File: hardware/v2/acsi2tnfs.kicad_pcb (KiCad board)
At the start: 2 copper layers, 51.5 x 60.2 mm, 22 parts, among them J1 Conn_01x19, J3 To SD card, SW1 SW_Prev, U1 SN74LVC245APW, U2 SN74LVC245APW, U3 SN74LS07

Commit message: Hardware: v2 and v2-cable, drop v1 and dev
v2 (DB19 on the board) and the new v2-cable (flat cable to a Lotharek DB19
adapter, pass-through header) share one circuit: 74LS07 for /IRQ and /DRQ,
pull-ups on /OE and the 74LS07 inputs, no pull-ups on /IRQ and /DRQ (those
upset the floppy drive when the board is off). v2-cable's box headers are
numbered per row, so pin n is ACSI pin n like on the adapter. Each project
carries its own footprints and fp-lib-table. hardware/README.md explains
both boards. v1, dev and the old gerbers are gone.

Co-Authored-By: Claude Opus 5.5 <noreply@anthropic.com>
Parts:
- removed R1, R2: NC, Resistor_SMD:R_0805_2012Metric
- J1: value Conn_01x19 -> To ACSI
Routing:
- net /DRQ: track 28.1 -> 22.4 mm
- net +5V: track 62.8 -> 57.8 mm
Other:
- board text added: "Atari ST ASCI netdrive & harddisk emulator"
- board text added: "https://retroloft.net/projects/acsi2tnfs"

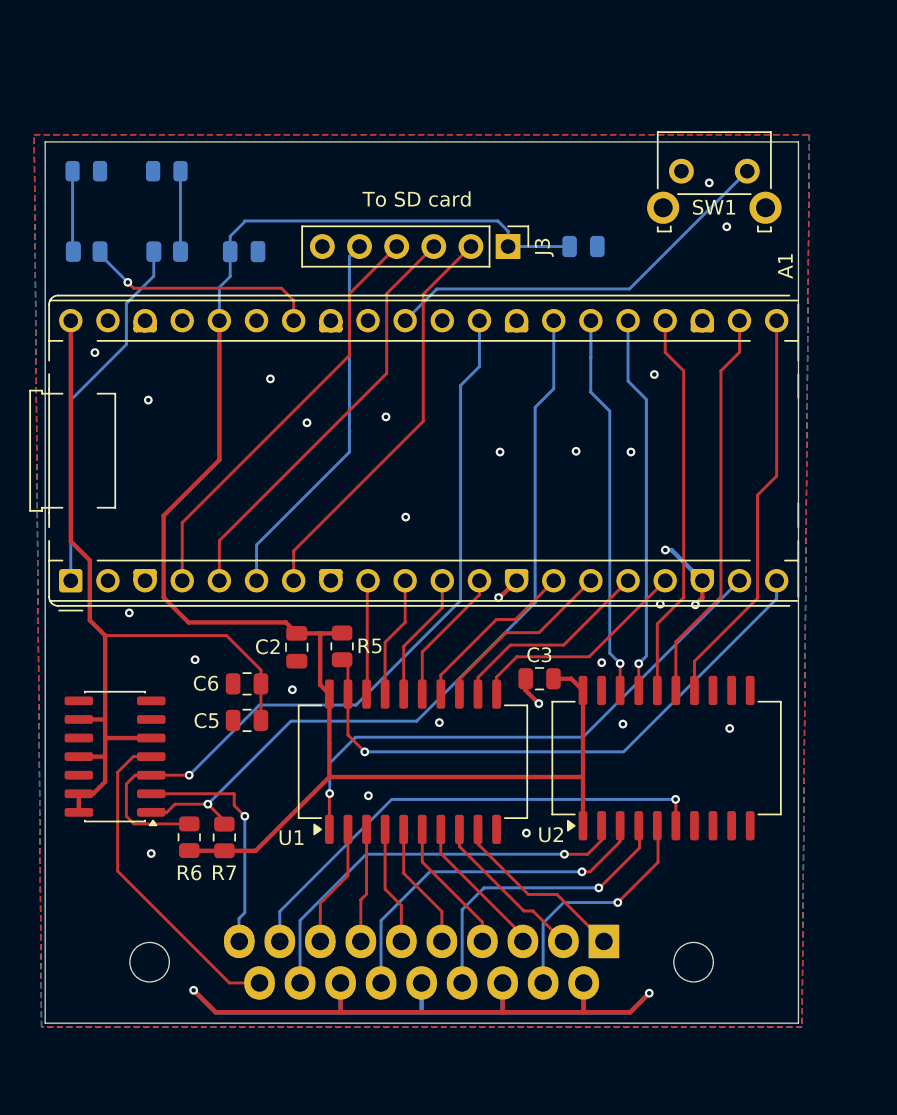
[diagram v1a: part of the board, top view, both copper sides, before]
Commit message: hardware/v2: TF-01A micro SD socket on the board, improved layout
Card1 uses the footprint from the project library; schema.pdf updated.

Co-Authored-By: Claude Opus 5.5 <noreply@anthropic.com>
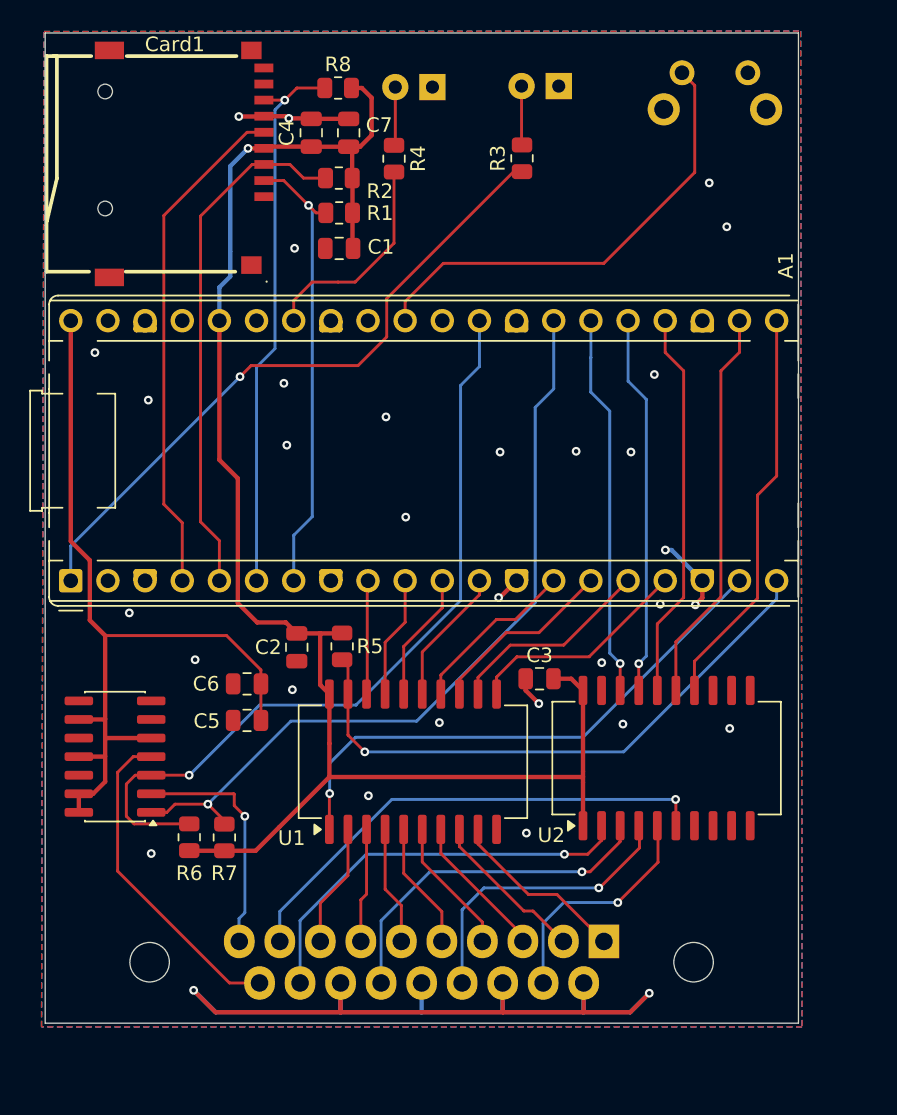
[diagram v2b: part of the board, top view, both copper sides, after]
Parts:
- removed J3: To SD card, Connector_PinHeader_2.54mm:PinHeader_1x06_P2.54mm_Vertical
- added C7: 10uF, Capacitor_SMD:C_0805_2012Metric, F.Cu at (131.0, 35.4)
- added Card1: TF-01A, ACSI Connector:TF-SMD_TF-01A, F.Cu at (119.9, 37.5)
- added R1: 10K, Resistor_SMD:R_0805_2012Metric, F.Cu at (130.3, 40.9)
- added R2: 10K, Resistor_SMD:R_0805_2012Metric, F.Cu at (130.3, 38.5)
- added R8: 10K, Resistor_SMD:R_0805_2012Metric, F.Cu at (130.3, 32.3)
- C1, R3, R4: moved to F.Cu
- C4: value 100n -> 100nF; moved to F.Cu
- D1, D2: footprint LED_SMD:LED_0805_2012Metric -> LED_THT:LED_D3.0mm
- SW1: moved to B.Cu
- moved D1 27.4 mm to (145.4, 32.2), turned to 180 degrees
- moved R3 25.1 mm to (142.8, 37.1), turned to -90 degrees
- moved D2 24.4 mm to (136.7, 32.2)
- moved R4 22.0 mm to (134.1, 37.1), turned to -90 degrees
- moved C4 20.2 mm to (128.4, 35.4), turned to 90 degrees
- moved SW1 8.12 mm to (158.3, 31.3), turned to 180 degrees
- moved C1 6.50 mm to (130.3, 43.3), turned to 180 degrees
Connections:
- A1 pad 4: CLK -> SCLK
- A1 pad 7: CS -> SD_CS
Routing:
- net SCLK: track 0.00 -> 34.7 mm
- net SD_CS: track 0.00 -> 31.4 mm, vias 0 -> 1
- net CLK: track 28.9 -> 0.00 mm
- net CS: track 27.9 -> 0.00 mm
- net POWER_LED: track 24.9 -> 45.4 mm, vias 0 -> 1
- net MISO: track 25.8 -> 38.2 mm, vias 0 -> 1
- net GND: track 88.5 -> 96.1 mm, vias 29 -> 32
- net MOSI: track 28.9 -> 35.9 mm
- net BUTTON: track 27.6 -> 31.9 mm
- net +3.3V: track 115.6 -> 111.3 mm, vias 0 -> 1
- net Net-(D2-A): track 5.52 -> 4.02 mm
- net Net-(D1-A): track 5.50 -> 4.04 mm
- net STATUS_LED: track 16.1 -> 14.7 mm, vias 1 -> 0
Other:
- board size 51.5 x 60.2 mm -> 51.5 x 67.7 mm
- board text added: "Mode"

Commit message: hardware: U1/U2 are 74LVC245ADW, silkscreen says ACSI
Both boards: the value of U1/U2 matches the SOIC-20W footprint, the
silkscreen text reads ACSI instead of ASCI, and a stray text outside the
v2 board is gone. schema.pdf and the 3D views updated.

Co-Authored-By: Claude Opus 5.5 <noreply@anthropic.com>
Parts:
- U1, U2: value SN74LVC245APW -> 74LVC245ADW
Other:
- board text added: "Atari ST ACSI netdrive & harddisk emulator"
- board text removed: "Atari ST ASCI netdrive & harddisk emulator"
- board text removed: "Atari ST ASCI netdrive and harddisk emulator"
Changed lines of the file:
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@@
 			)
 		)
-		(property "Value" "SN74LVC245APW"
+		(property "Value" "74LVC245ADW"
 			(at 0 8.66 90)
 			(layer "F.Fab")
@@
 			)
 		)
-		(property "Value" "SN74LVC245APW"
+		(property "Value" "74LVC245ADW"
 			(at 0 8.66 90)
 			(layer "F.Fab")
@@
 		(layer "Edge.Cuts")
 	)
-	(gr_text "Atari ST ASCI netdrive and harddisk emulator"
-		(at 200.5 144.5 0)
-		(layer "F.SilkS")
-		(effects
-			(font
-				(size 1.5 1.5)
-				(thickness 0.3)
-				(bold yes)
-			)
-			(justify left bottom)
-		)
-	)
 	(gr_text "Power"
 		(at 146.845 36.57 0)
@@
 		)
 	)
-	(gr_text "Atari ST ASCI netdrive & harddisk emulator"
+	(gr_text "Atari ST ACSI netdrive & harddisk emulator"
 		(at 160.95 56.05 0)
 		(layer "B.SilkS")

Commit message: hardware: D1 yellow, D2 blue, both on 470 ohm
R3 and R4 are 470 ohm in both boards; the led values name the colour
(v2-cable: D3 yellow, D4 blue as well). schema.pdf and the parts list
updated.

Co-Authored-By: Claude Opus 5.5 <noreply@anthropic.com>
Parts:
- D1: value LED -> LED yellow
- D2: value LED -> LED blue
- R3, R4: value 330 -> 470
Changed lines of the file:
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@@
 			)
 		)
-		(property "Value" "330"
+		(property "Value" "470"
 			(at -0.0325 -3.09 90)
 			(layer "F.Fab")
@@
 			)
 		)
-		(property "Value" "330"
+		(property "Value" "470"
 			(at 0.0725 3.06 90)
 			(layer "F.Fab")
@@
 			)
 		)
-		(property "Value" "LED"
+		(property "Value" "LED yellow"
 			(at 4.9575 -1.65 0)
 			(layer "B.Fab")
@@
 			)
 		)
-		(property "Value" "LED"
+		(property "Value" "LED blue"
 			(at 4.95 1.59 0)
 			(layer "B.Fab")
